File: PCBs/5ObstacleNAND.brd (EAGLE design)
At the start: 36.5 x 30.5 mm, 4 parts, among them IC1 74ALS00N, IC2 74LS32N

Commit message: updated something
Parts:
- added IC3: 7805DT, adafruit:TO252
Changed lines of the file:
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@@
 <drawing>
 <settings>
-<setting alwaysvectorfont="yes"/>
+<setting alwaysvectorfont="no"/>
 <setting verticaltext="up"/>
 </settings>
@@
 <layer number="56" name="wert" color="7" fill="1" visible="no" active="no"/>
 <layer number="57" name="tCAD" color="7" fill="1" visible="no" active="no"/>
+<layer number="59" name="tCarbon" color="7" fill="1" visible="no" active="no"/>
+<layer number="60" name="bCarbon" color="7" fill="1" visible="no" active="no"/>
 <layer number="88" name="SimResults" color="9" fill="1" visible="no" active="no"/>
 <layer number="89" name="SimProbes" color="9" fill="1" visible="no" active="no"/>
@@
 <layer number="113" name="IDFDebug" color="4" fill="1" visible="yes" active="yes"/>
 <layer number="116" name="Patch_BOT" color="9" fill="4" visible="yes" active="yes"/>
+<layer number="118" name="Rect_Pads" color="7" fill="1" visible="no" active="no"/>
 <layer number="121" name="_tsilk" color="7" fill="1" visible="yes" active="yes"/>
 <layer number="122" name="_bsilk" color="7" fill="1" visible="yes" active="yes"/>
@@
 <layer number="127" name="_tValues" color="7" fill="1" visible="yes" active="yes"/>
 <layer number="128" name="_bValues" color="7" fill="1" visible="yes" active="yes"/>
+<layer number="129" name="Mask" color="7" fill="1" visible="yes" active="yes"/>
 <layer number="131" name="tAdjust" color="7" fill="1" visible="yes" active="yes"/>
 <layer number="132" name="bAdjust" color="7" fill="1" visible="yes" active="yes"/>
@@
 <layer number="230" name="230bmp" color="7" fill="1" visible="yes" active="yes"/>
 <layer number="231" name="231bmp" color="7" fill="1" visible="yes" active="yes"/>
+<layer number="232" name="Eagle3D_PG2" color="7" fill="1" visible="no" active="no"/>
+<layer number="233" name="Eagle3D_PG3" color="7" fill="1" visible="no" active="no"/>
 <layer number="248" name="Housing" color="7" fill="1" visible="yes" active="yes"/>
 <layer number="249" name="Edge" color="7" fill="1" visible="yes" active="yes"/>
@@
 <layer number="251" name="SMDround" color="12" fill="11" visible="no" active="no"/>
 <layer number="254" name="cooling" color="7" fill="1" visible="yes" active="yes"/>
+<layer number="255" name="routoute" color="7" fill="1" visible="yes" active="yes"/>
 </layers>
 <board>
@@
 <attribute name="VALUE" x="41.9925" y="27.4325" size="1.016" layer="27" ratio="10" rot="R270"/>
 </element>
+<element name="IC3" library="adafruit" package="TO252" value="7805DT" x="2.54" y="10.16" smashed="yes">
+<attribute name="NAME" x="-1.27" y="7.62" size="1.27" layer="25" rot="R90"/>
+<attribute name="VALUE" x="7.62" y="7.62" size="1.27" layer="27" rot="R90"/>
+</element>
 </elements>

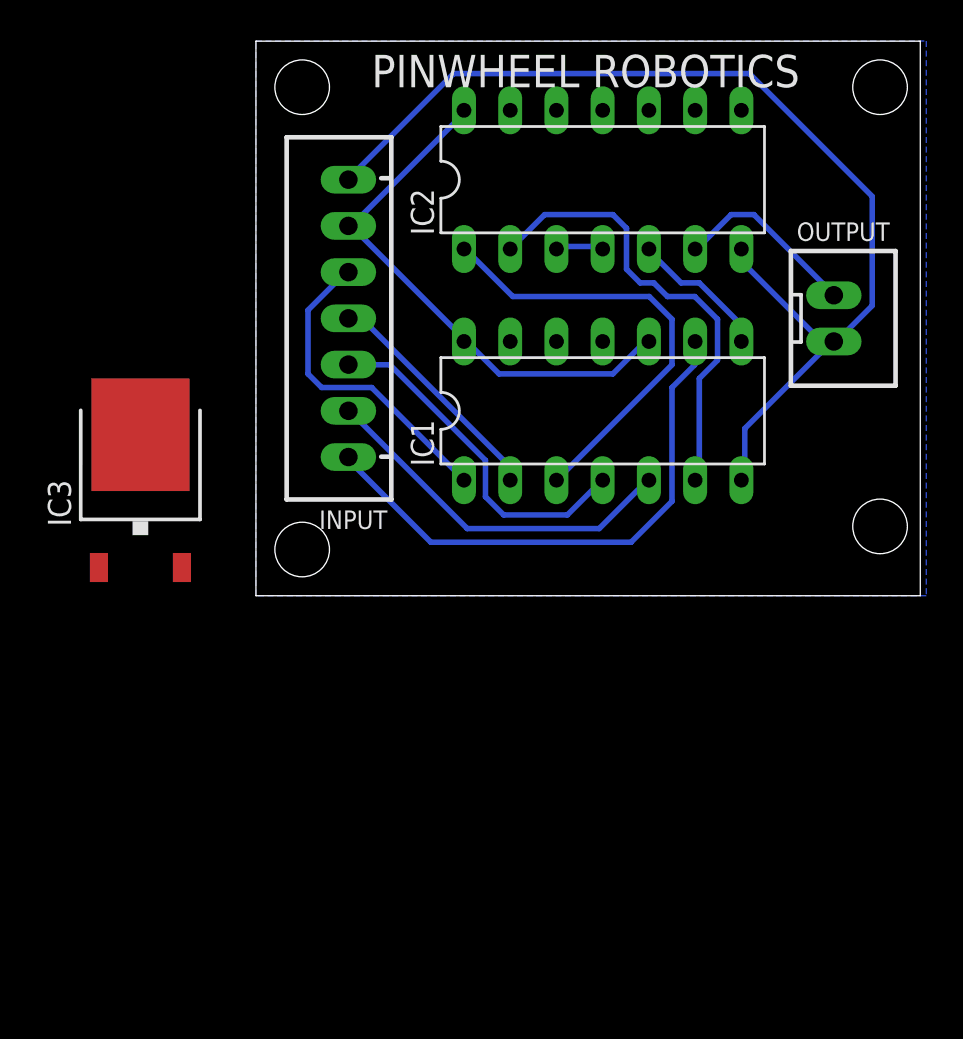
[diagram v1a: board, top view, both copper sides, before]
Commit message: Nand Gate Board updated
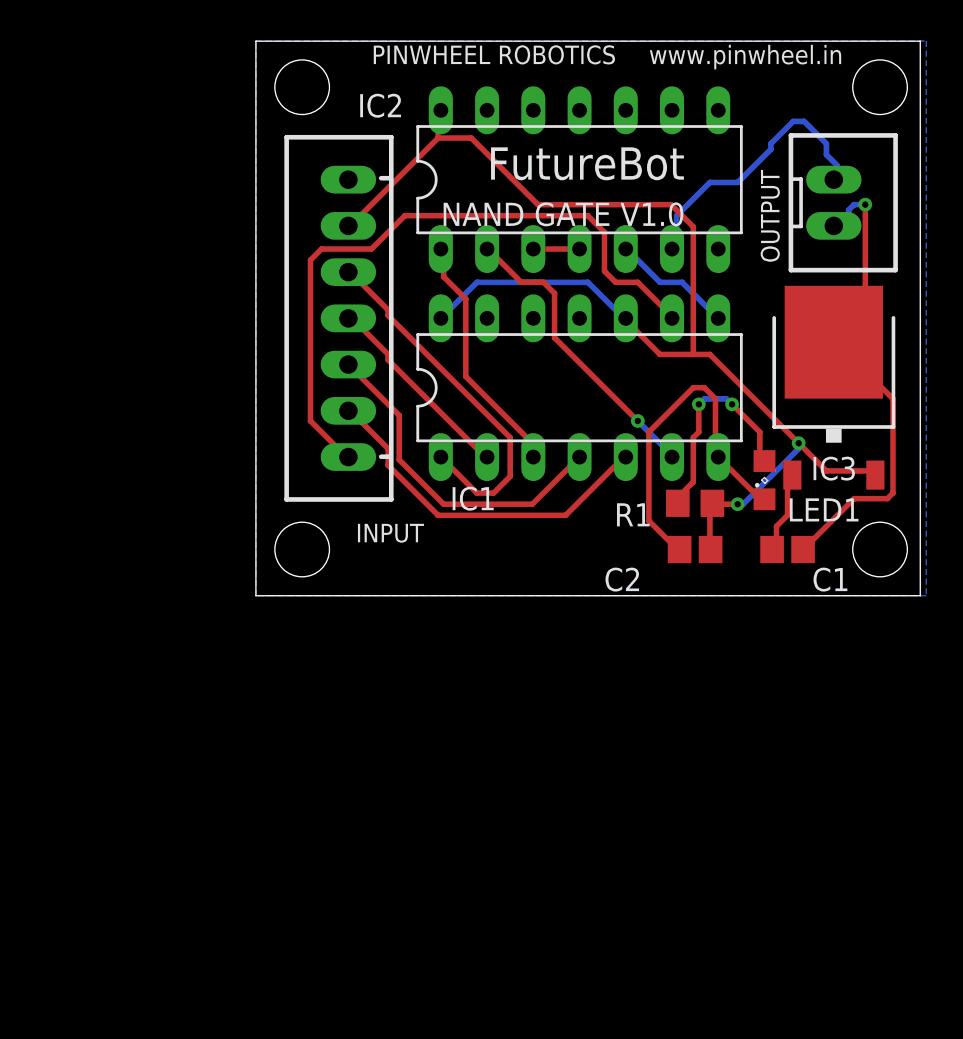
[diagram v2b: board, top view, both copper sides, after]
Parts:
- added C1: 0.22uF, adafruit:C0805
- added C2: 0.1uF, adafruit:C0805
- added LED1: 3mm, led:SML0805
- added R1: 330E, rcl:R0805
- moved IC3 38.4 mm to (40.6, 15.2)
- moved OUTPUT 6.35 mm to (40.6, 25.4)
- moved IC1 1.80 mm to (26.7, 15.2)
- moved IC2 1.27 mm to (26.7, 26.7)
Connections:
- new net N$12: LED1.A, R1.1
- new net N$13: C1.1, IC3.1
- net GND: now also C1.2, C2.2, IC3.3, LED1.C
- net VCC: now also C2.1, IC3.2, R1.2
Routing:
- net VCC: track 30.0 -> 69.8 mm, vias 0 -> 2
- net GND: track 60.6 -> 46.4 mm, vias 0 -> 1
- net N$12: track 0.00 -> 12.0 mm, vias 0 -> 2
- net N$6: track 24.5 -> 13.6 mm
- net N$7: track 25.3 -> 16.4 mm, vias 0 -> 1
- net N$5: track 30.0 -> 36.2 mm
- net N$10: track 10.2 -> 15.5 mm
- net N$13: track 0.00 -> 4.73 mm
- net N$1: track 17.6 -> 20.0 mm
- net N$2: track 13.0 -> 11.1 mm
- net N$9: track 7.75 -> 6.66 mm
- net N$3: track 19.3 -> 18.4 mm
- net N$4: track 20.3 -> 19.5 mm
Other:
- board text added: "17/11/2021"
- board text added: "Designed &manufacturd by"
- board text added: "Documentation at"
- board text added: "FutureBot"
- board text added: "FutureBot NAND Gate V1.0"
- board text added: "NAND GATE V1.0"
- board text added: "Pinwheel Robotics"
- board text added: "care@pinwheel.in"
- board text added: "www.pinwheel.in"

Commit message: added connector for Vin and 5V
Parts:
- added 5V, OUTPUT2: JST-XH-02-PIN-LONG-PAD, Rembrandt Electronics - JST XH Connectors v1-0:JST-XH-02-PACKAGE-LONG-PAD
- added VIN(7V-9V): (no value), con-wago-500:W237-102
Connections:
- net GND: now also 5V.2, OUTPUT2.2, VIN(7V-9V).2
- net N$13: now also VIN(7V-9V).1
- net VCC: now also OUTPUT2.1
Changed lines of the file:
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@@
 <drawing>
 <settings>
-<setting alwaysvectorfont="yes"/>
+<setting alwaysvectorfont="no"/>
 <setting verticaltext="up"/>
 </settings>
@@
 <attribute name="VALUE" x="32.385" y="6.35" size="1.27" layer="27"/>
 </element>
+<element name="VIN(7V-9V)" library="con-wago-500" library_urn="urn:adsk.eagle:library:195" package="W237-102" package3d_urn="urn:adsk.eagle:package:10688/1" value="" x="3.81" y="24.13" smashed="yes" rot="R90">
+<attribute name="MF" value="" x="3.81" y="24.13" size="1.778" layer="27" rot="R90" display="off"/>
+<attribute name="MPN" value="237-102" x="3.81" y="24.13" size="1.778" layer="27" rot="R90" display="off"/>
+<attribute name="NAME" x="8.8138" y="20.2838" size="1.27" layer="25" ratio="10" rot="R90"/>
+<attribute name="OC_FARNELL" value="unknown" x="3.81" y="24.13" size="1.778" layer="27" rot="R90" display="off"/>
+<attribute name="OC_NEWARK" value="70K9898" x="3.81" y="24.13" size="1.778" layer="27" rot="R90" display="off"/>
+<attribute name="POPULARITY" value="32" x="3.81" y="24.13" size="1.778" layer="27" rot="R90" display="off"/>
+<attribute name="VALUE" x="11.43" y="19.09" size="1.27" layer="27" ratio="10" rot="R90"/>
+</element>
+<element name="5V" library="Rembrandt Electronics - JST XH Connectors v1-0" package="JST-XH-02-PACKAGE-LONG-PAD" value="JST-XH-02-PIN-LONG-PAD" x="6.35" y="-3.81" smashed="yes">
+<attribute name="NAME" x="2.095" y="-5.85" size="1.016" layer="25" ratio="10" rot="R90"/>
+<attribute name="VALUE" x="3.0475" y="0.0825" size="1.016" layer="27" ratio="10"/>
+</element>
+<element name="OUTPUT2" library="Rembrandt Electronics - JST XH Connectors v1-0" package="JST-XH-02-PACKAGE-LONG-PAD" value="JST-XH-02-PIN-LONG-PAD" x="6.35" y="-12.7" smashed="yes">
+<attribute name="NAME" x="2.095" y="-14.74" size="1.016" layer="25" ratio="10" rot="R90"/>
+<attribute name="VALUE" x="3.0475" y="-8.8075" size="1.016" layer="27" ratio="10"/>
+</element>
 </elements>
 <signals>
@@
 <wire x1="40.8432" y1="17.9832" x2="40.64" y2="17.74" width="0.3048" layer="1"/>
 <via x="42.3672" y="25.2984" extent="1-16" drill="0.35"/>
+<contactref element="VIN(7V-9V)" pad="2"/>
+<contactref element="5V" pad="2"/>
+<contactref element="OUTPUT2" pad="2"/>
+<wire x1="40.64" y1="24.13" x2="34.29" y2="22.86" width="0" layer="19" extent="1-1"/>
+<wire x1="36.83" y1="9.11" x2="38.95" y2="6.35" width="0" layer="19" extent="1-1"/>
+<wire x1="13.97" y1="26.67" x2="34.29" y2="22.86" width="0" layer="19" extent="1-1"/>
+<wire x1="5.08" y1="26.63" x2="13.97" y2="26.67" width="0" layer="19" extent="1-1"/>
+<wire x1="7.62" y1="-3.81" x2="32.17" y2="6.35" width="0" layer="19" extent="1-1"/>
+<wire x1="7.62" y1="-12.7" x2="7.62" y2="-3.81" width="0" layer="19" extent="1-1"/>
 </signal>
 <signal name="VCC">
@@
 <via x="35.3568" y="8.8392" extent="1-16" drill="0.35"/>
 <via x="38.7096" y="12.192" extent="1-16" drill="0.35"/>
+<contactref element="OUTPUT2" pad="1"/>
+<wire x1="5.08" y1="-12.7" x2="33.87" y2="6.35" width="0" layer="19" extent="1-1"/>
 </signal>
 <signal name="N$1">
@@
 <wire x1="37.4904" y1="6.4008" x2="37.25" y2="6.35" width="0.3048" layer="1"/>
 <wire x1="38.1" y1="10.3632" x2="38.36" y2="10.44" width="0.3048" layer="1"/>
+<contactref element="VIN(7V-9V)" pad="1"/>
+<wire x1="5.08" y1="21.63" x2="38.36" y2="10.44" width="0" layer="19" extent="1-1"/>
 </signal>
 </signals>

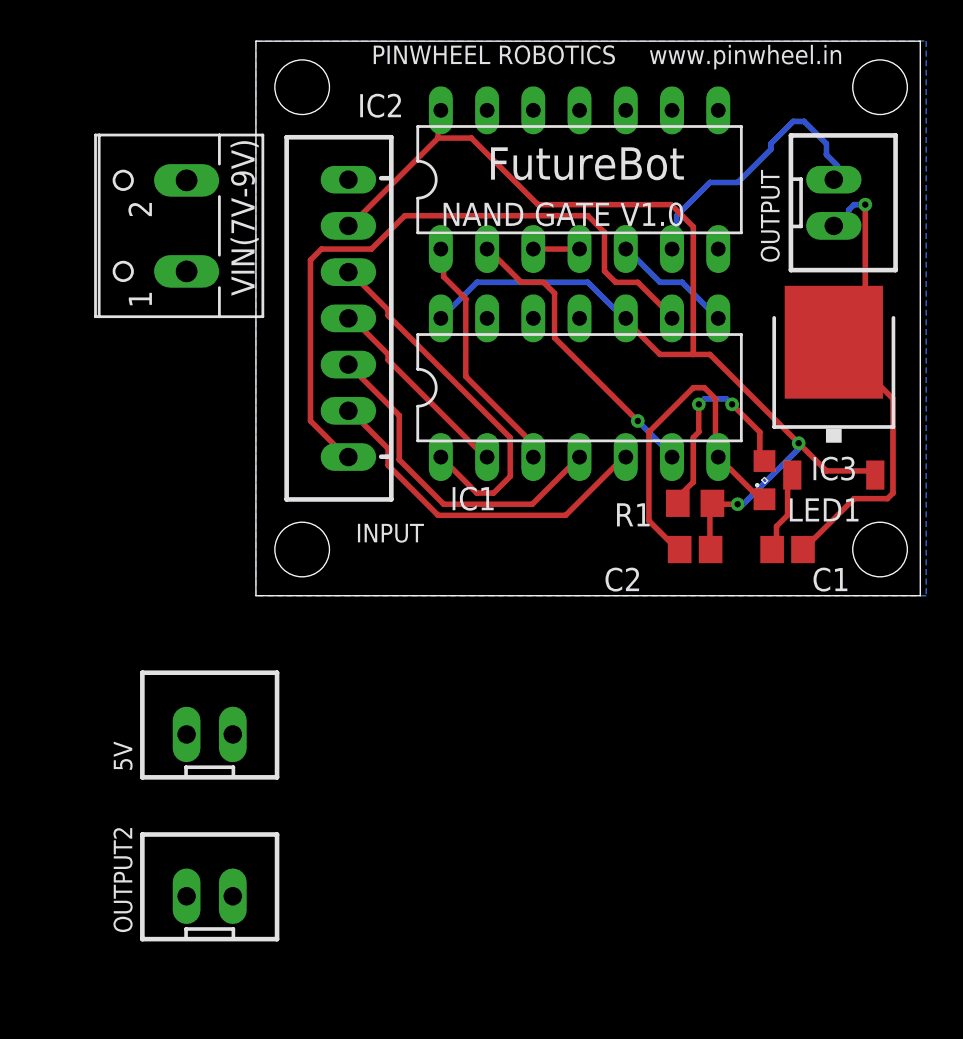
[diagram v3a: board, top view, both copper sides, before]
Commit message: updated nand gate amd nodmcu
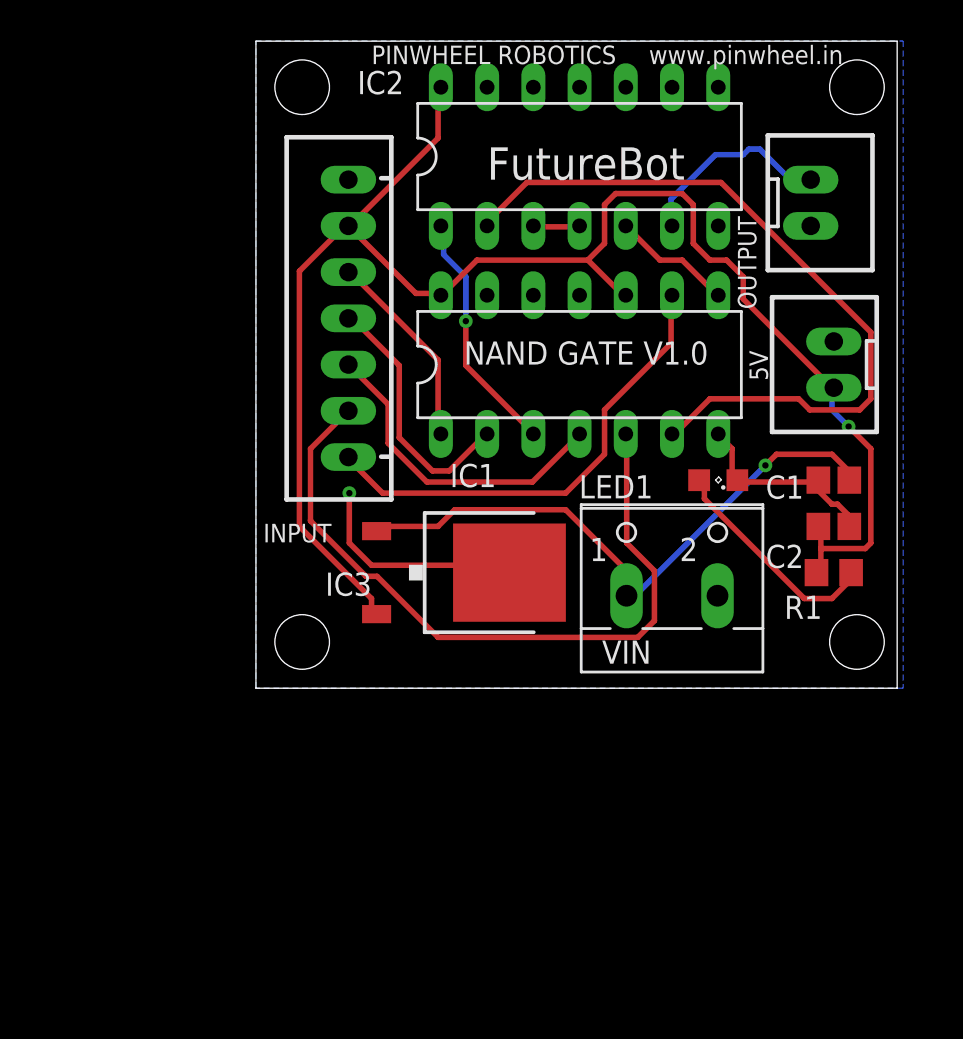
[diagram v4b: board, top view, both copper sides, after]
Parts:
- removed OUTPUT2: JST-XH-02-PIN-LONG-PAD, Rembrandt Electronics - JST XH Connectors v1-0:JST-XH-02-PACKAGE-LONG-PAD
- removed VIN(7V-9V): (no value), con-wago-500:W237-102
- added VIN: 7V-9v, con-wago-500:W237-102
- moved 5V 39.9 mm to (40.6, 16.5), turned to 90 degrees
- moved IC3 22.7 mm to (20.3, 5.08), turned to 270 degrees
- moved R1 8.52 mm to (40.6, 5.08), turned to 180 degrees
- moved C2 7.73 mm to (40.6, 7.62), turned to 0 degrees
- moved C1 4.58 mm to (40.6, 10.2), turned to 180 degrees
- moved LED1 2.54 mm to (34.3, 10.2), turned to 180 degrees
- moved OUTPUT 1.27 mm to (39.4, 25.4)
- moved IC1 1.27 mm to (26.7, 16.5)
- moved IC2 1.27 mm to (26.7, 27.9)
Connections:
- net GND: now also VIN.2; no longer OUTPUT2.2, VIN(7V-9V).2
- net N$13: now also VIN.1; no longer VIN(7V-9V).1
- net VCC: now also 5V.1; no longer OUTPUT2.1
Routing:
- net N$13: track 4.73 -> 33.6 mm, vias 0 -> 1
- net N$7: track 16.4 -> 41.4 mm, vias 1 -> 0
- net GND: track 46.4 -> 23.8 mm
- net VCC: track 69.8 -> 90.4 mm, vias 2 -> 1
- net N$4: track 19.5 -> 39.7 mm
- net N$5: track 36.2 -> 26.1 mm
- net N$1: track 20.0 -> 11.1 mm
- net N$10: track 15.5 -> 11.0 mm
- net N$2: track 11.1 -> 14.4 mm
- net N$3: track 18.4 -> 17.7 mm
- net N$12: track 12.0 -> 12.5 mm, vias 2 -> 0
- net N$6: vias 0 -> 1
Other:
- board size 36.5 x 30.5 mm -> 35.2 x 35.6 mm
- board text added: "Designed & Manufacturd by Pinwheel Robotics 17/11/2021 FutureBot NAND Gate Shield V1.0"
- board text added: "Documentation at www.pinwheel.in"
- board text removed: "17/11/2021"
- board text removed: "Designed &manufacturd by"
- board text removed: "Documentation at"
- board text removed: "FutureBot NAND Gate V1.0"
- board text removed: "Pinwheel Robotics"

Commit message: updated
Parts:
- added LED2: Green, led:SML0805
- added R2: 10K, rcl:R0805
- added R3: 330E, rcl:R0805
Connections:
- new net N$11: LED2.C, R3.1
- net GND: now also R2.1, R3.2
- net N$10: now also LED2.A, R2.2
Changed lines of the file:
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@@
 <drawing>
 <settings>
-<setting alwaysvectorfont="yes"/>
+<setting alwaysvectorfont="no"/>
 <setting verticaltext="up"/>
 </settings>
@@
 <attribute name="VALUE" x="36.7475" y="13.2075" size="1.016" layer="27" ratio="10" rot="R90"/>
 </element>
+<element name="R2" library="rcl" library_urn="urn:adsk.eagle:library:334" package="R0805" package3d_urn="urn:adsk.eagle:package:23553/2" value="10K" x="11.43" y="-5.08" smashed="yes">
+<attribute name="NAME" x="10.795" y="-3.81" size="1.27" layer="25"/>
+<attribute name="POPULARITY" value="85" x="11.43" y="-5.08" size="1.778" layer="27" display="off"/>
+<attribute name="SPICEPREFIX" value="R" x="11.43" y="-5.08" size="1.778" layer="27" display="off"/>
+<attribute name="VALUE" x="10.795" y="-7.62" size="1.27" layer="27"/>
+</element>
+<element name="LED2" library="led" library_urn="urn:adsk.eagle:library:259" package="SML0805" package3d_urn="urn:adsk.eagle:package:15830/1" value="Green" x="11.43" y="-11.43" smashed="yes">
+<attribute name="NAME" x="9.93" y="-10.43" size="1.27" layer="25"/>
+<attribute name="POPULARITY" value="17" x="11.43" y="-11.43" size="1.778" layer="27" display="off"/>
+<attribute name="VALUE" x="9.93" y="-13.43" size="1.27" layer="27"/>
+</element>
+<element name="R3" library="rcl" library_urn="urn:adsk.eagle:library:334" package="R0805" package3d_urn="urn:adsk.eagle:package:23553/2" value="330E" x="11.43" y="-17.78" smashed="yes">
+<attribute name="NAME" x="10.795" y="-16.51" size="1.27" layer="25"/>
+<attribute name="POPULARITY" value="85" x="11.43" y="-17.78" size="1.778" layer="27" display="off"/>
+<attribute name="SPICEPREFIX" value="R" x="11.43" y="-17.78" size="1.778" layer="27" display="off"/>
+<attribute name="VALUE" x="10.795" y="-20.32" size="1.27" layer="27"/>
+</element>
 </elements>
 <signals>
@@
 <wire x1="22.5552" y1="5.1816" x2="22.82" y2="5.08" width="0.3048" layer="1"/>
 <via x="14.0208" y="9.4488" extent="1-16" drill="0.35"/>
+<contactref element="R2" pad="1"/>
+<contactref element="R3" pad="2"/>
+<wire x1="34.29" y1="24.13" x2="39.37" y2="24.13" width="0" layer="19" extent="1-1"/>
+<wire x1="40.64" y1="17.78" x2="39.37" y2="24.13" width="0" layer="19" extent="1-1"/>
+<wire x1="39.79" y1="10.16" x2="40.64" y2="17.78" width="0" layer="19" extent="1-1"/>
+<wire x1="34.25" y1="3.81" x2="35.34" y2="10.16" width="0" layer="19" extent="1-1"/>
+<wire x1="22.82" y1="5.08" x2="34.25" y2="3.81" width="0" layer="19" extent="1-1"/>
+<wire x1="10.48" y1="-5.08" x2="14.0208" y2="9.4488" width="0" layer="19" extent="1-1"/>
+<wire x1="12.38" y1="-17.78" x2="10.48" y2="-5.08" width="0" layer="19" extent="1-1"/>
+<wire x1="13.97" y1="26.67" x2="14.0208" y2="9.4488" width="0" layer="19" extent="1-1"/>
 </signal>
 <signal name="VCC">
@@
 <wire x1="31.6992" y1="24.384" x2="31.75" y2="24.13" width="0.3048" layer="16"/>
 <wire x1="39.3192" y1="26.8224" x2="39.37" y2="26.67" width="0.3048" layer="16"/>
+<contactref element="R2" pad="2"/>
+<contactref element="LED2" pad="A"/>
+<wire x1="12.38" y1="-5.08" x2="31.75" y2="24.13" width="0" layer="19" extent="1-1"/>
+<wire x1="12.48" y1="-11.43" x2="12.38" y2="-5.08" width="0" layer="19" extent="1-1"/>
 </signal>
 <signal name="N$12">
@@
 <via x="36.8808" y="10.9728" extent="1-16" drill="0.35"/>
 </signal>
+<signal name="N$11">
+<contactref element="LED2" pad="C"/>
+<contactref element="R3" pad="1"/>
+<wire x1="10.38" y1="-11.43" x2="10.48" y2="-17.78" width="0" layer="19" extent="1-1"/>
+</signal>
 </signals>

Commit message: updated
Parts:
- moved R3 27.9 mm to (22.9, 7.62), turned to 180 degrees
- moved LED2 20.1 mm to (17.8, 7.62)
- moved R2 11.4 mm to (11.4, 6.35), turned to 90 degrees
- moved IC3 2.54 mm to (20.3, 2.54)
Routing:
- net GND: track 23.8 -> 118.0 mm
- net N$10: track 11.0 -> 61.3 mm, vias 0 -> 1
- net VCC: track 90.4 -> 125.6 mm
- net N$7: track 41.4 -> 19.2 mm
- net N$4: track 39.7 -> 18.4 mm
- net N$5: track 26.1 -> 42.2 mm
- net N$11: track 0.00 -> 8.63 mm
- net N$13: track 33.6 -> 31.7 mm, vias 1 -> 2
- net N$6: vias 1 -> 0
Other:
- board text added: "Designed & Manufacturd by Pinwheel Robotics 27/11/2021 FutureBot NAND Gate Shield V1.0"
- board text removed: "Designed & Manufacturd by Pinwheel Robotics 17/11/2021 FutureBot NAND Gate Shield V1.0"
